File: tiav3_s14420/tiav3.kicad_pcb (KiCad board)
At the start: 4 copper layers, 25.3 x 25.3 mm, 21 parts, among them J1 SSQ-103-01-G-D, J2 Conn_Coaxial, U1 OPA847IDBVT

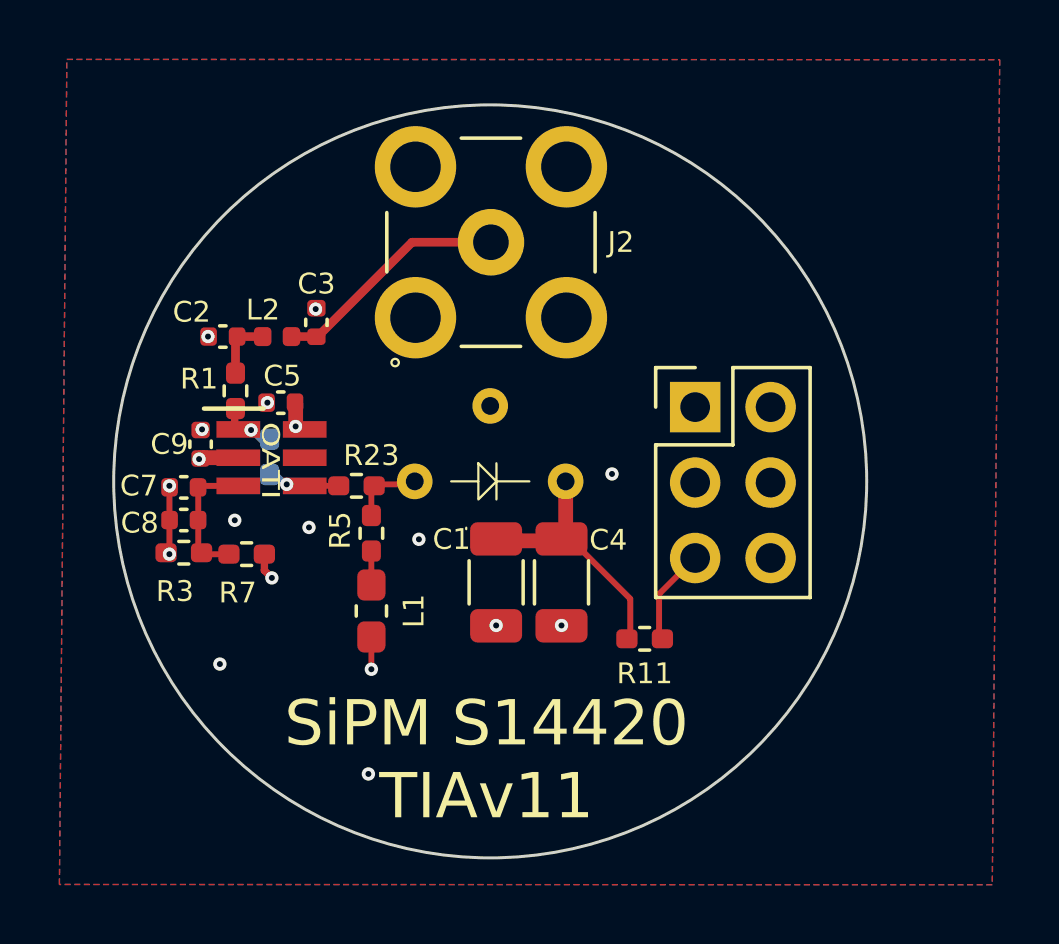
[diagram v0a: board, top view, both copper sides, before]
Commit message: Switch all TIA boards to 0603 for the low pass inductor
0402 is fine for higher cutoffs but its hard to find >1000nH in 0402 without having high resistance.
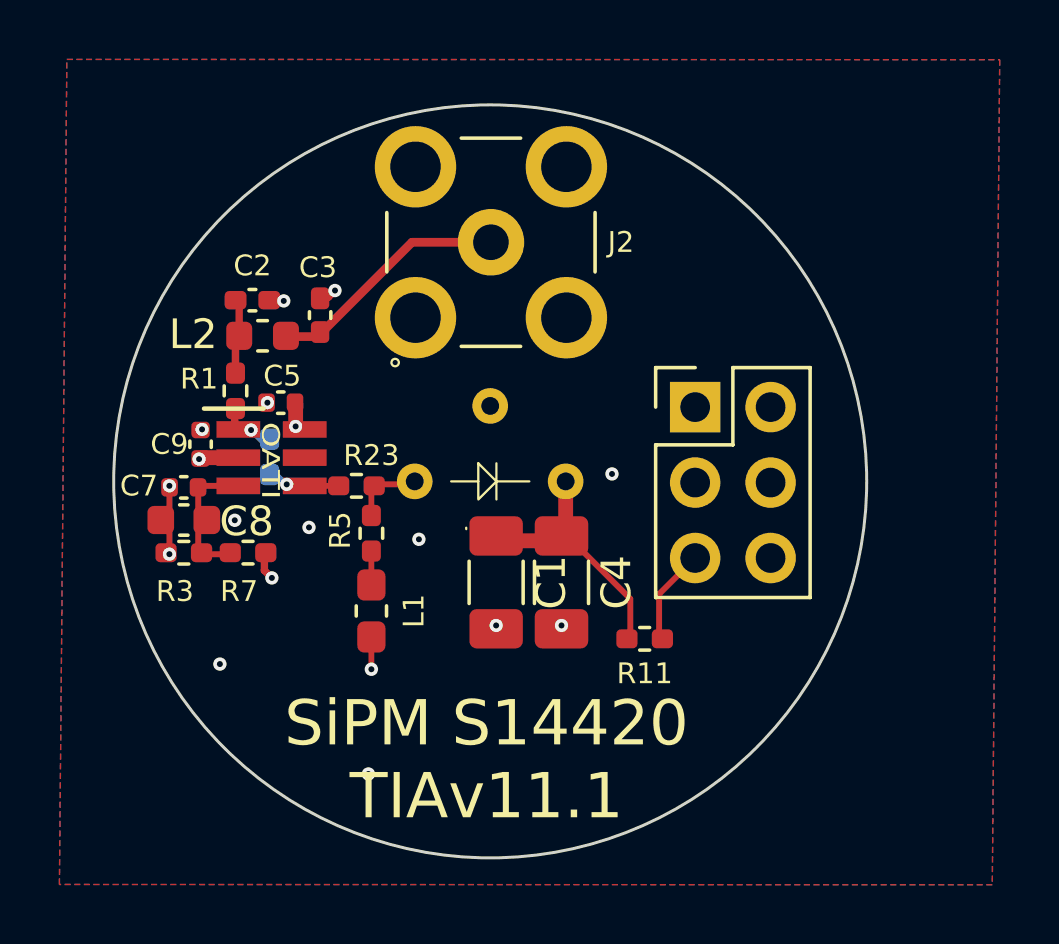
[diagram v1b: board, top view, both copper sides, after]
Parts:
- C1, C4: footprint Resistor_SMD:R_1206_3216Metric -> Capacitor_SMD:C_1206_3216Metric_Pad1.33x1.80mm_HandSolder
- C2: footprint Capacitor_SMD:C_0402_1005Metric -> Capacitor_SMD:C_0402_1005Metric_Pad0.74x0.62mm_HandSolder
- C3: value 330p -> 330pF; footprint Capacitor_SMD:C_0402_1005Metric -> Capacitor_SMD:C_0402_1005Metric_Pad0.74x0.62mm_HandSolder
- C8: value 1u -> 22u; footprint Capacitor_SMD:C_0402_1005Metric -> Capacitor_SMD:C_0603_1608Metric
- L2: footprint Inductor_SMD:L_0402_1005Metric -> Inductor_SMD:L_0603_1608Metric
- moved C2 1.58 mm to (192.0, 93.9), turned to 0 degrees
- moved L2 0.49 mm to (192.3, 95.1)
- moved C3 0.28 mm to (194.3, 94.4)
- moved R7 0.07 mm to (191.8, 102.4)
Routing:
- net GND: track 3.48 -> 4.80 mm
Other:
- board text added: "SiPM S14420 TIAv11.1"
- board text removed: "SiPM S14420 TIAv11"
